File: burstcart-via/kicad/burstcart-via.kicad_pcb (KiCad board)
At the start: 2 copper layers, 56 x 91 mm, 24 parts, among them J1 IEC, J3 BURST, J4 PORTB, U1 27C512, U2 74LS74, U3 6522, U4 22V10, U5 74LS126

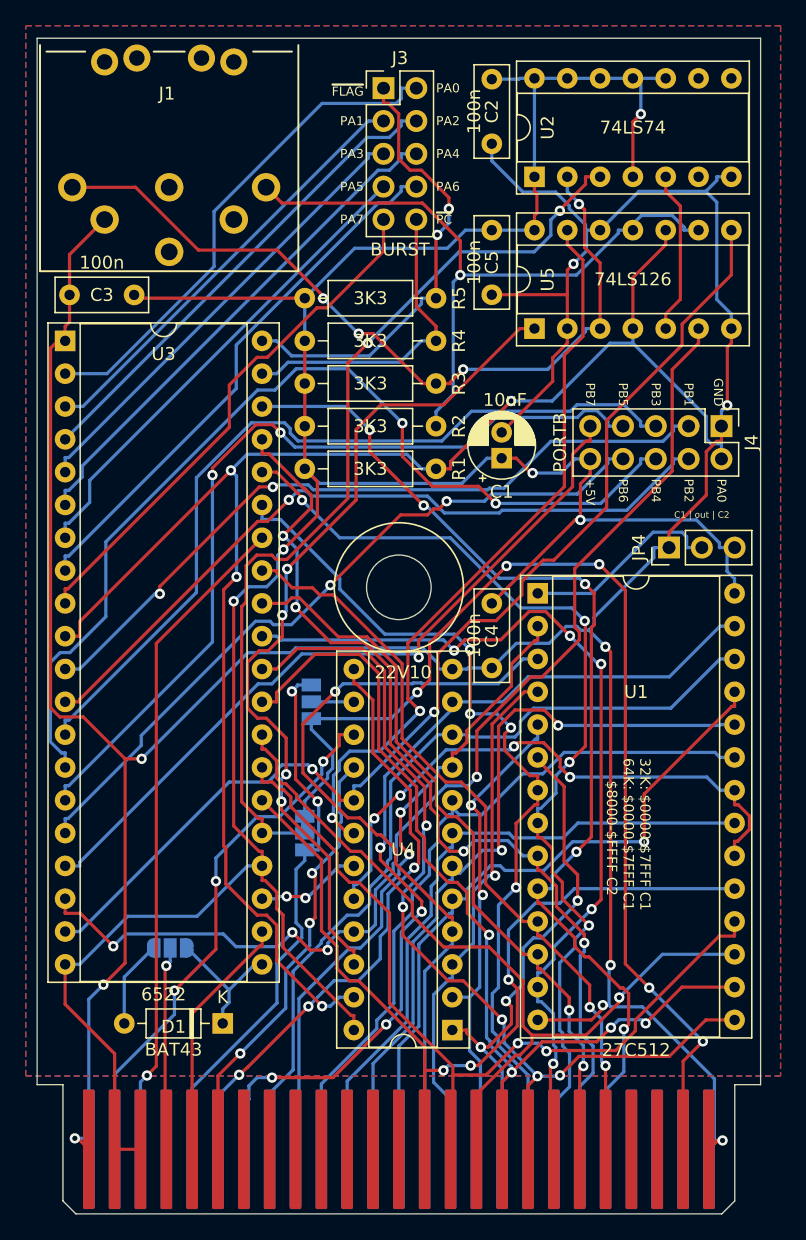
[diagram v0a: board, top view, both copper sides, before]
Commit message: corrected JP4 to connect to Phi0 by default, corrected silkscreen texts ; updated to KiCad9
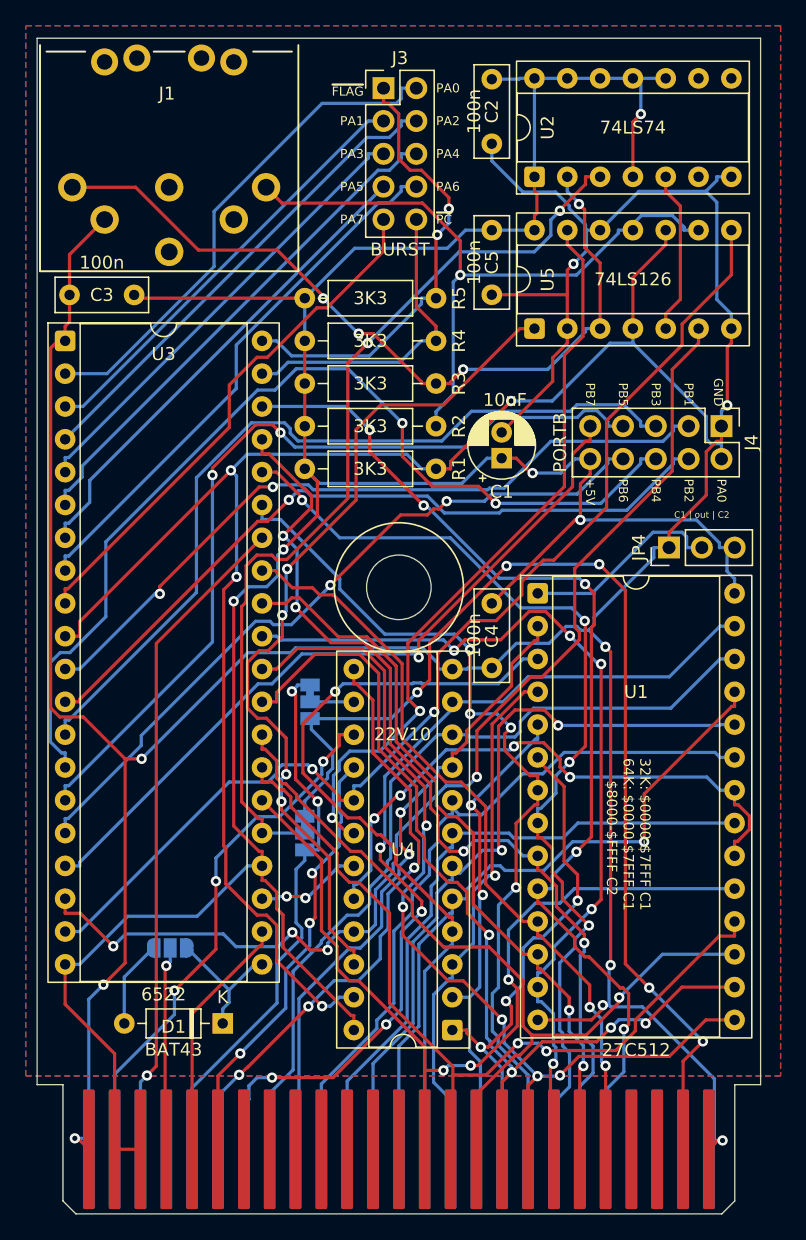
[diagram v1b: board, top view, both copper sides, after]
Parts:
- C2, C3, C4, C5: value 470p -> 100n
- JP3: footprint Jumper:SolderJumper-3_P1.3mm_Open_Pad1.0x1.5mm_NumberLabels -> Jumper:SolderJumper-3_P1.3mm_Bridged12_Pad1.0x1.5mm_NumberLabels
- moved JP3 0.10 mm to (141.4, 103.1), turned to -90 degrees
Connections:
- JP3 pad 1: /PHI2 -> /PHI0
- JP3 pad 3: /PHI0 -> /PHI2
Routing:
- net /A13: track 64.0 -> 59.7 mm
- net /D5: track 64.0 -> 59.8 mm
- net /A15: track 46.9 -> 42.8 mm
- net /A14: track 71.9 -> 67.9 mm
- net /A2: track 76.3 -> 72.4 mm
- net /A6: track 40.5 -> 36.6 mm
- net VCC: track 223.4 -> 221.2 mm
- net GND: track 266.1 -> 264.7 mm
- net IEC_SRQ: track 62.1 -> 61.5 mm
- net Net-(D1-K): track 10.8 -> 10.2 mm
- net IEC_DATA: track 53.4 -> 52.9 mm
- net /A9: track 58.3 -> 57.7 mm
- net /A11: track 55.6 -> 55.0 mm
- net /SPout: track 58.4 -> 57.9 mm
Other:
- board text added: "1-2: W65C22S 3-2: other"
- board text added: "BurstCart+4 v1.1b Maciej <ytm@elysium.pl> Witkowiak, VII 2025"
- board text removed: "3-2: W65C22S 1-2: other"
- board text removed: "BurstCart+4 v1.1 Maciej <ytm@elysium.pl> Witkowiak, V 2025"
